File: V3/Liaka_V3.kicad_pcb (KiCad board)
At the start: 4 copper layers, 101.6 x 26.9 mm, 64 parts, among them J1 SPI_Interface_Male, J2 USB_B_Micro, J3 RRC3, J4 THD2528-11SD-GF, J6 Conn_Coaxial, J7 FTDI_Female, J8 I2C_Interface_Male, J9 2-3S_LiPo_LARGE_HOLE_XT-30, Q1 Si2301CDS, Q2 MMBT2222, Q3 MMBT2222, Q4 MMBT2222, SW1 BOOT, U1 ESP32-WROOM-32, U2 AMS1117-3.3, U3 MS5611, U4 CP2102N-A01-GQFN28, U5 L80-M39, U6 MPU-6050, U7 RFM95W-915S2

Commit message: Added sims, updated V3 board
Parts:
- removed BOOT: RESET, Button_Switch_SMD:SW_Push_1P1T_NO_CK_KSC6xxJ
- removed BUZZER: Conn_01x02_Female, Connector_PinSocket_2.54mm:PinSocket_1x02_P2.54mm_Vertical
- removed C17: 100uF, Capacitor_Tantalum_SMD:CP_EIA-3528-21_Kemet-B
- removed C18: 10uF, Capacitor_Tantalum_SMD:CP_EIA-3216-18_Kemet-A
- removed G***: LOGO, hpr-library:logo-18mm
- removed J8: I2C_Interface_Male, Connector_PinHeader_2.54mm:PinHeader_1x04_P2.54mm_Vertical
- removed J9: 2-3S_LiPo_LARGE_HOLE_XT-30, Connector_AMASS:AMASS_XT30PW-M_1x02_P2.50mm_Horizontal
- removed REF** (x4): MountingHole_3.2mm_M3_ISO14580, MountingHole:MountingHole_3.2mm_M3_ISO14580
- removed REF**: Liaka_Text, footprints:Liaka_Text
- added D6: LED_RED, LED_SMD:LED_0603_1608Metric, F.Cu at (30.5, 52.7)
- added H1: MountingHole, MountingHole:MountingHole_3.2mm_M3_ISO14580_Pad_TopOnly, F.Cu at (128.0, 84.0)
- added H2: MountingHole, MountingHole:MountingHole_3.2mm_M3_ISO14580_Pad_TopOnly, F.Cu at (128.0, 105.0)
- added H3: MountingHole, MountingHole:MountingHole_3.2mm_M3_ISO14580_Pad_TopOnly, F.Cu at (189.2, 84.0)
- added H4: MountingHole, MountingHole:MountingHole_3.2mm_M3_ISO14580_Pad_TopOnly, F.Cu at (189.2, 105.0)
- added IC1: XTSD04GLGEAG, Local_footprints:SON127P800X600X95-8N, B.Cu at (152.9, 94.3)
- added J5: USB_B_Micro, Connector_USB:USB_Micro-B_Molex-105017-0001, F.Cu at (135.5, 104.5)
- added Q5: MMBT2222, Package_TO_SOT_SMD:SOT-23, F.Cu at (53.1, 67.4)
- added Q6: MMBT2222, Package_TO_SOT_SMD:SOT-23, F.Cu at (-7.37, 86.2)
- added R14: 1k, Resistor_SMD:R_0603_1608Metric, F.Cu at (-2.92, 87.8)
- added R15: 10k, Resistor_SMD:R_0603_1608Metric, F.Cu at (191.3, 100.3)
- added R16: 2.4k, Resistor_SMD:R_0603_1608Metric, F.Cu at (15.8, 71.5)
- added R17: 2.4k, Resistor_SMD:R_0603_1608Metric, F.Cu at (1.13, 85.2)
- added R18: 1k, Resistor_SMD:R_0603_1608Metric, F.Cu at (1.13, 87.7)
- added R19: 300k, Resistor_SMD:R_0603_1608Metric, F.Cu at (25.9, 62.3)
- added R20: 100k, Resistor_SMD:R_0603_1608Metric, F.Cu at (25.9, 59.8)
- added R21: 10k, Resistor_SMD:R_0603_1608Metric, F.Cu at (191.2, 98.8)
- added SW2: RST, Button_Switch_SMD:SW_Push_1P1T_NO_CK_KSC6xxJ, F.Cu at (203.5, 94.6)
- added SW3: BOOT, Button_Switch_SMD:SW_Push_1P1T_NO_CK_KSC6xxJ, F.Cu at (194.3, 94.6)
- added SW4: SD_DUMP, Button_Switch_SMD:SW_Push_1P1T_NO_CK_KSC6xxJ, F.Cu at (203.5, 86.4)
- added U8: CP2102N-A01-GQFN28, Package_DFN_QFN:QFN-28-1EP_5x5mm_P0.5mm_EP3.35x3.35mm, F.Cu at (136.8, 98.0)
- added U9: ESP32-WROOM-32, RF_Module:ESP32-WROOM-32, F.Cu at (172.9, 97.5)
- C1, C4: value 10uF -> 100nF
- C11: value 2.2nF -> 1uF
- C12: value 10uF -> 1uF
- C13, C16: value 0.1uF -> 100nF
- C14, C3, C9: value 100nF -> 10uF
- C15: value 10uF -> 100uF; footprint Capacitor_SMD:C_0603_1608Metric -> Capacitor_Tantalum_SMD:CP_EIA-3528-21_Kemet-B
- C2: value 1uF -> 100nF
- C5: value 1uF -> 10uF
- C6: value 10nF -> 10uF; footprint Capacitor_SMD:C_0603_1608Metric -> Capacitor_Tantalum_SMD:CP_EIA-3216-18_Kemet-A
- C8: value 100nF -> 100uF; footprint Capacitor_SMD:C_0603_1608Metric -> Capacitor_Tantalum_SMD:CP_EIA-3528-21_Kemet-B
- D1: value LED_RED -> LED_BLUE
- D2: value LED_BLUE -> B5819W; footprint LED_SMD:LED_0603_1608Metric -> Diode_SMD:D_SOD-123
- D4: value ERROR_STATUS_LED -> B5819W; footprint LED_SMD:LED_0603_1608Metric -> Diode_SMD:D_SOD-123
- D5: value B5819W -> ERROR_STATUS_LED; footprint Diode_SMD:D_SOD-123 -> LED_SMD:LED_0603_1608Metric
- J1: value SPI_Interface_Male -> Conn_Coaxial; footprint Connector_PinHeader_2.54mm:PinHeader_1x04_P2.54mm_Vertical -> Connector_Coaxial:SMA_Amphenol_132291_Vertical
- J2: value USB_B_Micro -> 2-3S_LiPo_LARGE_HOLE_XT-30; footprint Connector_USB:USB_Micro-B_Molex-105017-0001 -> Connector_AMASS:AMASS_XT30PW-M_1x02_P2.50mm_Horizontal
- J3: value RRC3 -> RRC3_In
- J4: value THD2528-11SD-GF -> I2C_Interface_Male; footprint footprints:THD252811SDGF -> Connector_PinHeader_2.54mm:PinHeader_1x04_P2.54mm_Vertical; moved to F.Cu
- J6: value Conn_Coaxial -> Conn_01x02_Female; footprint Connector_Coaxial:SMA_Amphenol_132291_Vertical -> Connector_PinSocket_2.54mm:PinSocket_1x02_P2.54mm_Vertical
- J7: value FTDI_Female -> THD2528-11SD-GF; footprint Connector_PinHeader_2.54mm:PinHeader_1x05_P2.54mm_Vertical -> Local_footprints:THD252811SDGF; moved to B.Cu
- Q2: value MMBT2222 -> Si2301CDS; footprint Package_TO_SOT_SMD:SOT-23_Handsoldering -> Package_TO_SOT_SMD:SOT-23; moved to F.Cu
- Q3: value MMBT2222 -> Si2301CDS; footprint Package_TO_SOT_SMD:SOT-23_Handsoldering -> Package_TO_SOT_SMD:SOT-23
- Q4: footprint Package_TO_SOT_SMD:SOT-23_Handsoldering -> Package_TO_SOT_SMD:SOT-23
- R1: value 10k -> 1k
- R11: value 10k -> 12k
- R12: value 30k -> 10k
- R2: value 10k -> 50k
- R3: value 1k -> 5.1M
- R4: value 1k -> 3M
- R5: value 1k -> 100k
- R6: value 2.4k -> 3M
- R7: value 2.4k -> 1M
- R8: value 10k -> 100k
- R9: value 12k -> 100k
- SW1: value BOOT -> SW_SPDT; footprint Button_Switch_SMD:SW_Push_1P1T_NO_CK_KSC6xxJ -> Local_footprints:SSSS811101; moved to B.Cu
- U1: value ESP32-WROOM-32 -> L80-M39; footprint RF_Module:ESP32-WROOM-32 -> Local_footprints:L80-M39
- U2: value AMS1117-3.3 -> MS561101BA03-50; footprint Package_TO_SOT_SMD:SOT-223-3_TabPin2 -> Local_footprints:MS561101BA03-50; moved to B.Cu
- U3: value MS5611 -> ADXL375BCCZ-RL7; footprint footprints:MS561101BA03-50 -> Local_footprints:ADXL375BCCZ-RL7
- U4: value CP2102N-A01-GQFN28 -> RFM95W-915S2; footprint Package_DFN_QFN:QFN-28-1EP_5x5mm_P0.5mm_EP3.35x3.35mm -> RF_Module:HOPERF_RFM9XW_SMD; moved to B.Cu
- U5: value L80-M39 -> LM393; footprint XCVR_L80-M39:XCVR_L80-M39 -> Local_footprints:LM393DR2G; moved to B.Cu
- U6: value MPU-6050 -> ADR5040ARTZ-2.048; footprint footprints:MPU-6050 -> Local_footprints:Analog_Devices-ADR5040ARTZ-REEL7-Level_C; moved to B.Cu
- U7: value RFM95W-915S2 -> AMS1117-3.3; footprint RF_Module:HOPERF_RFM9XW_SMD -> Package_TO_SOT_SMD:SOT-223-3_TabPin2; moved to F.Cu
- moved J6 176.6 mm to (26.2, 53.7)
- moved D5 169.5 mm to (-2.88, 85.3)
- moved R13 145.4 mm to (34.5, 55.3), turned to 0 degrees
- moved C12 143.8 mm to (21.5, 68.2)
- moved Q4 134.9 mm to (48.4, 72.4)
- moved C14 130.3 mm to (30.5, 57.8)
- moved D4 108.0 mm to (16.6, 68.6)
- moved R12 103.8 mm to (59.9, 59.8), turned to 0 degrees
- moved R11 99.5 mm to (63.9, 59.8)
- moved C11 99.1 mm to (59.9, 62.3)
- moved C13 98.0 mm to (30.5, 55.3), turned to 0 degrees
- moved D1 88.7 mm to (79.6, 70.9)
- moved R1 76.6 mm to (83.6, 70.9)
- moved C2 75.4 mm to (83.6, 73.5), turned to 0 degrees
- moved J4 75.3 mm to (48.3, 60.3), turned to 0 degrees
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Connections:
- C10 pad 1: Net-(C10-Pad1) -> VDD
- C11 pad 1: Net-(C11-Pad1) -> VDD
- C12 pad 1: VDD -> EN
- C2 pad 1: EN -> VDD
- C7 pad 1: GND -> Net-(C7-Pad1)
- C7 pad 2: Net-(C7-Pad2) -> GND
- D2 pad 1: GND -> Net-(C7-Pad1)
- D2 pad 2: Net-(D2-Pad2) -> +5V
- D3 pad 1: Net-(C10-Pad1) -> VDC
- D3 pad 2: +5V -> Net-(D3-Pad2)
- D4 pad 1: GND -> VDD
- D5 pad 1: VDD -> GND
- J1 pad 1: CS_RF -> Net-(J1-Pad1)
- J1 pad 2: MISO_RF -> GND
- J2 pad 1: +5V -> GND
- J2 pad 2: Net-(J2-Pad2) -> +BATT
- J3 pad 1: +BATT -> VDC
- J4 pad 1: Net-(J4-Pad1) -> SDA
- J4 pad 2: CS_SD -> SCL
- J4 pad 3: MOSI_SD -> VDD
- J4 pad 4: VDD -> GND
- J6 pad 1: Net-(J6-Pad1) -> VDD
- J6 pad 2: GND -> Net-(D4-Pad2)
- J7 pad 1: DTR -> unconnected-(J7-Pad1)
- J7 pad 2: TXD0 -> CS_SD
- J7 pad 3: RXD0 -> MOSI_SD
- J7 pad 5: GND -> CLK_SD
- Q1 pad 2: Net-(C10-Pad1) -> Net-(C7-Pad1)
- Q1 pad 3: +BATT -> VCC
- Q2 pad 2: EN -> VCC
- Q2 pad 3: RTS -> VDC
- Q3 pad 1: Net-(Q3-Pad1) -> Net-(D3-Pad2)
- Q3 pad 2: BOOT -> VDC
- Q3 pad 3: DTR -> +BATT
- Q4 pad 2: Net-(D5-Pad2) -> EN
- Q4 pad 3: GND -> RTS
- R1 pad 1: VDD -> Net-(R1-Pad1)
- R1 pad 2: EN -> Net-(D1-Pad2)
- R10 pad 1: RTS -> DTR
- R10 pad 2: Net-(Q3-Pad1) -> Net-(Q4-Pad1)
- R11 pad 1: Batt_sense -> RTS
- R11 pad 2: GND -> Net-(Q5-Pad1)
- R12 pad 1: +BATT -> VDD
- R12 pad 2: Batt_sense -> Net-(R12-Pad2)
- R13 pad 1: Net-(Q4-Pad1) -> Net-(Q6-Pad1)
- R2 pad 1: GND -> /Power/Vp
- R2 pad 2: +5V -> VDC
- R3 pad 1: ESP_LED -> /Power/2s
- R3 pad 2: Net-(D4-Pad2) -> VDC
- R4 pad 1: VDD -> GND
- R4 pad 2: Net-(D1-Pad2) -> /Power/2s
- R5 pad 1: Net-(R5-Pad1) -> GND
- R5 pad 2: Net-(D2-Pad2) -> +5V
- R6 pad 1: VDD -> /Power/3s
- R6 pad 2: SDA -> VDC
- R7 pad 1: VDD -> GND
- R7 pad 2: SCL -> /Power/3s
- R8 pad 1: VDD -> Net-(Q2-Pad1)
- R8 pad 2: Net-(R8-Pad2) -> VDC
- R9 pad 1: DTR -> GND
- R9 pad 2: Net-(Q2-Pad1) -> Net-(D3-Pad2)
- SW1 pad 1: BOOT -> /Power/3s
- SW1 pad 2: GND -> Net-(SW1-Pad2)
- U1 pad 1: GND -> TXD2_GPS
- U1 pad 10: RF_IO2 -> VDD
- U1 pad 11: RF_IO1 -> unconnected-(U1-Pad11)
- U1 pad 12: RF_IO0 -> GND
- U1 pad 2: VDD -> RXD2_GPS
- U1 pad 3: EN -> GND
- U1 pad 4: Thermal_Probe -> VDD
- U1 pad 5: Batt_sense -> VDD
- U1 pad 6: RXD1_RRC3 -> Net-(R1-Pad1)
- U1 pad 7: RXD2_GPS -> unconnected-(U1-Pad7)
- U1 pad 8: ESP_LED -> unconnected-(U1-Pad8)
- U1 pad 9: BUZZER -> (no net)
- U2 pad 1: GND -> VDD
- U2 pad 3: Net-(C10-Pad1) -> GND
- U3 pad 1: VDD -> unconnected-(U3-Pad1)
- U3 pad 2: VDD -> GND
- U3 pad 3: GND -> unconnected-(U3-Pad3)
- U3 pad 6: Net-(U3-Pad6) -> unconnected-(U3-Pad6)
- U3 pad 7: SDA -> unconnected-(U3-Pad7)
- U3 pad 8: SCL -> unconnected-(U3-Pad8)
- U4 pad 1: Net-(U4-Pad1) -> GND
- U4 pad 10: Net-(U4-Pad10) -> GND
- U4 pad 11: Net-(U4-Pad11) -> unconnected-(U4-Pad11)
- U4 pad 12: Net-(U4-Pad12) -> unconnected-(U4-Pad12)
- U4 pad 13: Net-(U4-Pad13) -> VDD
- U4 pad 14: Net-(U4-Pad14) -> RF_IO0
- U4 pad 15: Net-(U4-Pad15) -> RF_IO1
- U4 pad 16: Net-(U4-Pad16) -> RF_IO2
- U4 pad 2: Net-(U4-Pad2) -> MISO_RF
- U4 pad 3: GND -> MOSI_RF
- U4 pad 4: Net-(J2-Pad3) -> SCK_RF
- U4 pad 5: Net-(J2-Pad2) -> CS_RF
- U4 pad 6: VDD -> RESET_RF
- U4 pad 7: VDD -> unconnected-(U4-Pad7)
- U4 pad 8: +5V -> GND
- U4 pad 9: Net-(R8-Pad2) -> Net-(J1-Pad1)
- U5 pad 1: TXD2_GPS -> Net-(Q2-Pad1)
- U5 pad 2: RXD2_GPS -> Net-(SW1-Pad2)
- U5 pad 3: GND -> /Power/Vp
- U5 pad 4: VDD -> GND
- U5 pad 5: VDD -> (no net)
- U5 pad 6: Net-(R5-Pad1) -> (no net)
- U5 pad 7: Net-(U5-Pad7) -> (no net)
- U5 pad 8: Net-(U5-Pad8) -> VDC
- U6 pad 1: GND -> /Power/Vp
- U6 pad 2: Net-(U6-Pad2) -> GND
- U6 pad 3: Net-(U6-Pad3) -> (no net)
- U7 pad 2: MISO_RF -> VDD
- U7 pad 3: MOSI_RF -> Net-(C7-Pad1)
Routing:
- net +BATT: track 138.9 -> 0.00 mm, vias 6 -> 0
- net SDA: track 133.7 -> 0.00 mm, vias 7 -> 0
- net SCL: track 128.0 -> 0.00 mm, vias 6 -> 0
- net DTR: track 110.1 -> 0.00 mm, vias 4 -> 0
- net GND: track 102.5 -> 0.00 mm, vias 35 -> 0
- net MISO_RF: track 89.3 -> 0.00 mm, vias 1 -> 0
- net CS_RF: track 86.1 -> 0.00 mm, vias 1 -> 0
- net MOSI_RF: track 75.5 -> 0.00 mm, vias 3 -> 0
- net SCK_RF: track 75.4 -> 0.00 mm, vias 3 -> 0
- net RXD0: track 74.7 -> 0.00 mm, vias 2 -> 0
- net TXD0: track 73.0 -> 0.00 mm, vias 1 -> 0
- net RESET_RF: track 72.6 -> 0.00 mm, vias 3 -> 0
- net EN: track 67.7 -> 0.00 mm, vias 5 -> 0
- net TXD1_RRC3: track 54.0 -> 0.00 mm, vias 4 -> 0
- net +5V: track 52.9 -> 0.00 mm, vias 3 -> 0
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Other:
- outline, holes or cut-outs redrawn

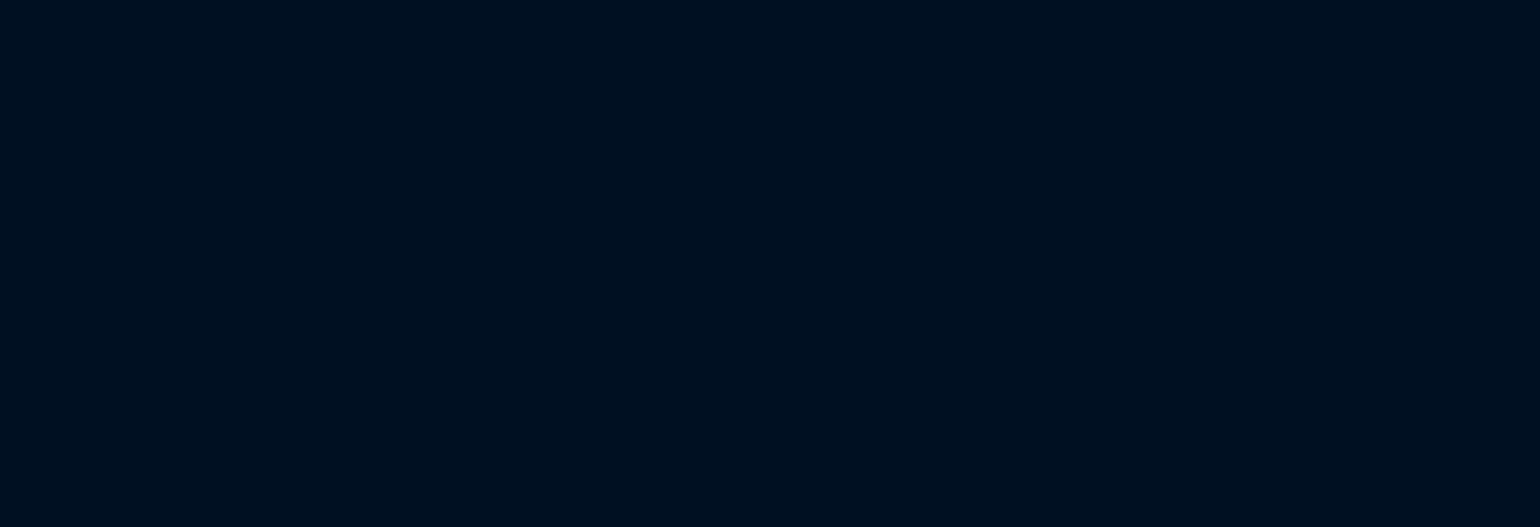
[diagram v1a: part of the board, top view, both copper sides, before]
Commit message: Added mpu6050 back
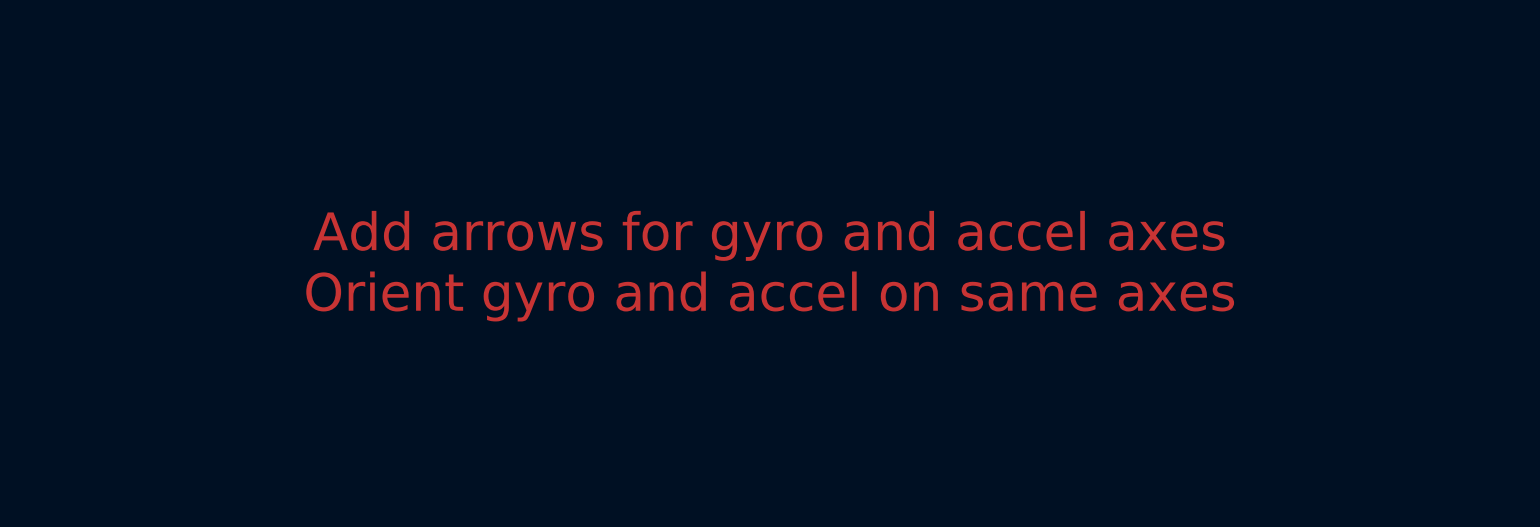
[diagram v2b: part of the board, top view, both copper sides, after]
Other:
- board text added: "Add arrows for gyro and accel axes Orient gyro and accel on same axes"
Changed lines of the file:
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@@
   (gr_arc locked (start 106.68 83.312) (mid 107.275159 81.875159) (end 108.712 81.28) (layer "Edge.Cuts") (width 0.15))
   (gr_line locked (start 208.28 83.312) (end 208.28 106.172) (layer "Edge.Cuts") (width 0.15))
+  (gr_text "Add arrows for gyro and accel axes\nOrient gyro and accel on same axes" (at 188.976 66.04) (layer "F.Cu")
+    (effects (font (size 1.5 1.5) (thickness 0.3)))
+  )
   (gr_text "2-3s LiPo" (at 255.651 75.4126 90) (layer "F.SilkS")
     (effects (font (size 1.3 1.3) (thickness 0.2)))

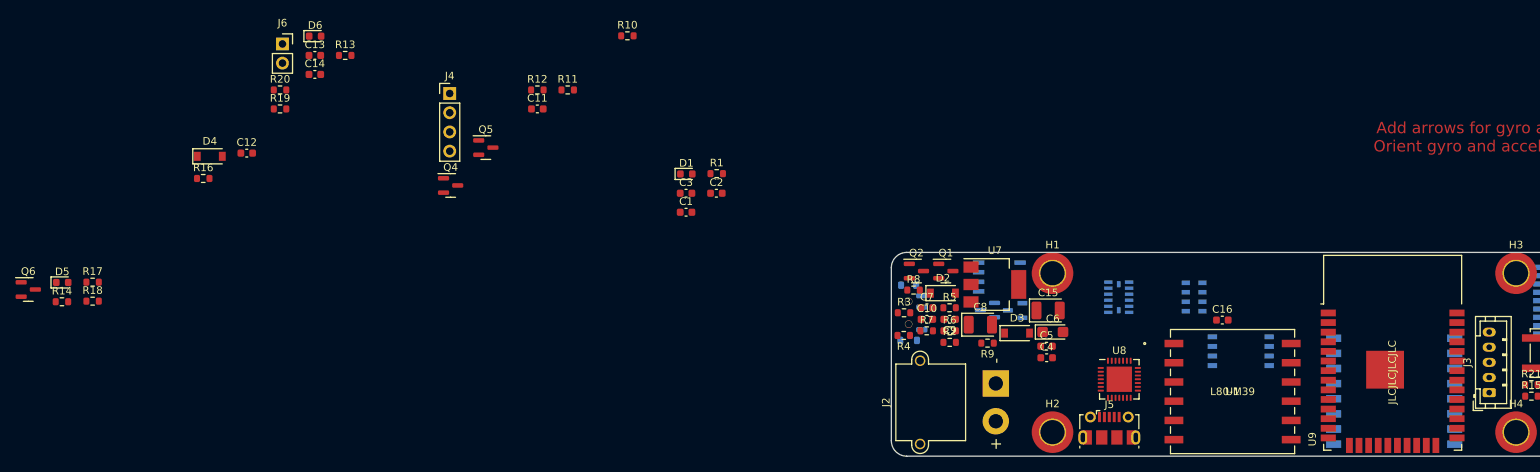
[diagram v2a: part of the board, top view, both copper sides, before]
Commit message: almost finished component placement
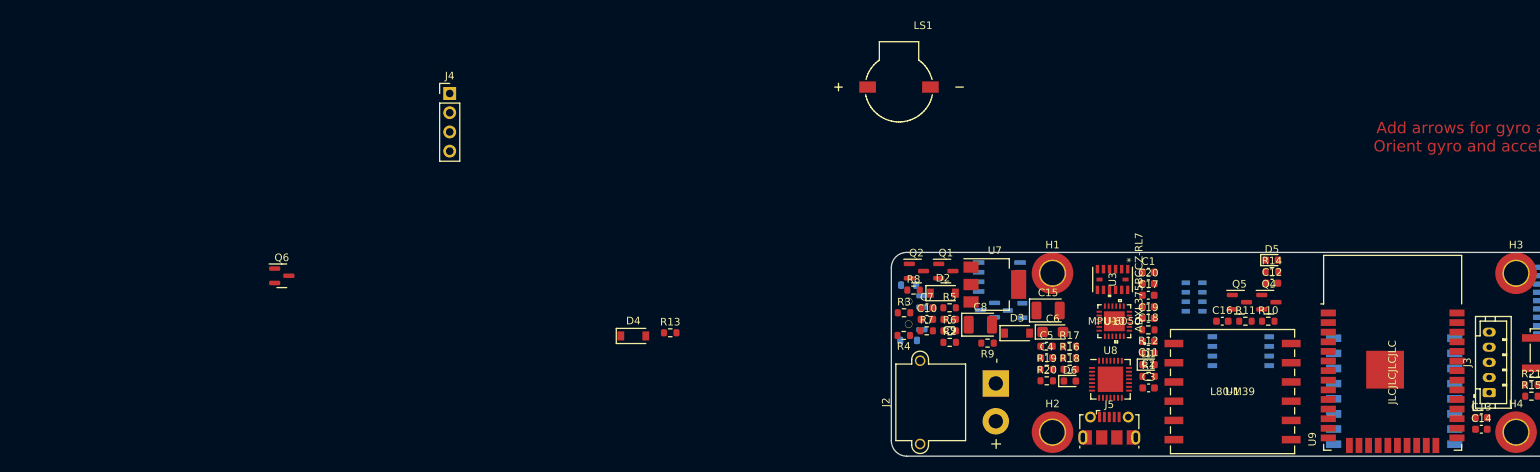
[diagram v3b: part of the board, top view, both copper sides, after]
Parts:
- removed J6: Conn_01x02_Female, Connector_PinSocket_2.54mm:PinSocket_1x02_P2.54mm_Vertical
- added C17: 10nF, Capacitor_SMD:C_0603_1608Metric, F.Cu at (140.6, 86.9)
- added C18: 0.1uF, Capacitor_SMD:C_0603_1608Metric, F.Cu at (140.6, 88.5)
- added C19: 2.2nF, Capacitor_SMD:C_0603_1608Metric, F.Cu at (140.6, 90.0)
- added C20: 0.1uF, Capacitor_SMD:C_0603_1608Metric, F.Cu at (140.6, 85.4)
- added LS1: SMT-1127-S-R, Local_footprints:XDCR_SMT-1127-S-R, F.Cu at (107.7, 59.4)
- added U10: MPU-6050, Local_footprints:MPU-6050, F.Cu at (136.1, 90.4)
- Q6: value MMBT2222 -> 2N7002
- U3: moved to F.Cu
- moved C13 161.4 mm to (184.6, 103.1)
- moved C14 161.1 mm to (184.6, 104.6)
- moved R14 159.9 mm to (157.0, 83.8)
- moved D5 159.9 mm to (157.0, 82.3)
- moved C12 136.6 mm to (157.0, 85.3)
- moved R18 129.4 mm to (130.3, 96.7)
- moved R17 129.4 mm to (130.2, 93.7)
- moved R16 116.9 mm to (130.2, 95.2)
- moved D6 109.7 mm to (130.3, 98.3)
- moved Q4 109.2 mm to (156.6, 87.9)
- moved R20 108.4 mm to (127.2, 98.2)
- moved R19 107.0 mm to (127.2, 96.7)
- moved Q5 101.7 mm to (152.7, 87.9)
- moved R11 94.6 mm to (153.5, 90.4)
- moved R10 92.7 mm to (156.5, 90.4)
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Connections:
- Q6 pad 2: Net-(D4-Pad2) -> GND
- Q6 pad 3: GND -> Net-(D4-Pad2)
- U3 pad 1: unconnected-(U3-Pad1) -> VDD
- U3 pad 12: unconnected-(U3-Pad12) -> GND
- U3 pad 6: unconnected-(U3-Pad6) -> VDD
- U3 pad 7: unconnected-(U3-Pad7) -> VDD
- U4 pad 15: RF_IO1 -> unconnected-(U4-Pad15)
- U4 pad 16: RF_IO2 -> unconnected-(U4-Pad16)
- U9 pad 10: RF_IO2 -> IO25
- U9 pad 11: RF_IO1 -> IO26

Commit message: Updated costing sheet:
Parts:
- added H5: HPR_Logo, Local_footprints:HPR_Logo, B.Cu at (152.6, 98.5)
- added H6: Liaka_Text, Local_footprints:Liaka_Text, B.Cu at (173.9, 88.4)
- moved J4 152.3 mm to (195.7, 98.6)
- moved Q6 130.4 mm to (156.6, 84.4)
- moved R13 85.0 mm to (162.3, 95.7), turned to -90 degrees
- moved D4 68.4 mm to (140.5, 84.0)
- moved LS1 48.3 mm to (147.7, 86.5)
- moved C16 12.1 mm to (162.3, 92.7), turned to -90 degrees
- moved SW3 11.4 mm to (203.5, 87.8), turned to 180 degrees
- moved U2 10.6 mm to (136.1, 86.9)
- moved IC1 9.87 mm to (149.8, 84.9)
- moved SW4 9.32 mm to (195.5, 91.2), turned to 90 degrees
- moved Q5 7.96 mm to (160.5, 89.5)
- moved D5 3.55 mm to (160.5, 82.2)
- moved C12 3.55 mm to (160.5, 85.2)
- moved R14 3.55 mm to (160.5, 83.7)
- moved C1 2.06 mm to (140.6, 86.0)
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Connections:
- J3 pad 1: VDC -> unconnected-(J3-Pad1)
- U10 pad 25: unconnected-(U10-Pad25) -> GND
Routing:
- net SDA: track 0.00 -> 96.3 mm, vias 0 -> 5
- net SCL: track 0.00 -> 94.2 mm, vias 0 -> 5
- net EN: track 0.00 -> 75.8 mm, vias 0 -> 6
- net MISO_SD: track 0.00 -> 73.0 mm, vias 0 -> 2
- net GND: track 0.00 -> 72.5 mm, vias 0 -> 50
- net BOOT: track 0.00 -> 66.2 mm, vias 0 -> 5
- net VDD: track 0.00 -> 63.1 mm, vias 0 -> 27
- net CLK_SD: track 0.00 -> 60.9 mm, vias 0 -> 2
- net Batt_sense: track 0.00 -> 53.8 mm, vias 0 -> 5
- net VDC: track 0.00 -> 51.5 mm, vias 0 -> 6
- net MOSI_SD: track 0.00 -> 51.1 mm, vias 0 -> 2
- net RXD0: track 0.00 -> 50.5 mm, vias 0 -> 2
- net TXD0: track 0.00 -> 49.6 mm, vias 0 -> 2
- net SD_DUMP: track 0.00 -> 46.8 mm, vias 0 -> 2
- net CS_XT: track 0.00 -> 45.6 mm, vias 0 -> 1
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- added copper zone on B.Cu, net GND
- added copper zone on F.Cu, net GND
- added copper zone on In2.Cu, net GND
- added copper zone on In1.Cu, net VDD
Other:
- rule pad_to_mask_clearance: 0.05 -> 0
- board text added: "2s"
- board text added: "3s"
- board text added: "Designed by Angus McLennan March 2022"
- board text added: "GND"
- board text added: "MS5611"
- board text added: "RRC3"
- board text added: "SCL"
- board text added: "SDA"
- board text added: "V3"
- board text added: "VDD"
- board text added: "XTSD04GLGEAG"
- board text added: "x"
- board text added: "y"
- board text added: "z"
- board text removed: "Add arrows for gyro and accel axes Orient gyro and accel on same axes"
